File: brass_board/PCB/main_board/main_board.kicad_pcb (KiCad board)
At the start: 2 copper layers, 76 parts, among them J1 Conn_POS_input_B, J10 Conn_Galvo_B, J2 Conn_POS_input_A, J6 Conn_ADC, J8 Conn_01x03_Male_Power, J9 Conn_Galvo_A, Q1 2N2219, U1 LM393, U10 Teensy4.0, U11 Teensy4.0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

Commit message: Added Arduino
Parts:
- added A1: Arduino_Nano_v3.x, Module:Arduino_Nano, F.Cu at (125.9, 146.9)
- added Q2: 2N2219, Package_TO_SOT_THT:TO-39-3, F.Cu at (146.1, 147.8)

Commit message: Added test points and line driver for laser trigger
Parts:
- added J14: Conn_POS_input_A, Connector_PinHeader_2.54mm:PinHeader_1x03_P2.54mm_Vertical, F.Cu at (105.4, 149.3)
- added J15: Conn_POS_input_B, Connector_PinHeader_2.54mm:PinHeader_1x03_P2.54mm_Vertical, F.Cu at (110.0, 149.3)
- added J16: Conn_02x02_Odd_Even, Connector_PinHeader_2.54mm:PinHeader_2x02_P2.54mm_Vertical, F.Cu at (115.0, 126.0)
- added J17: Conn_02x02_Odd_Even, Connector_PinHeader_2.54mm:PinHeader_2x02_P2.54mm_Vertical, F.Cu at (33.6, 87.8)
- added J18: Conn_02x02_Odd_Even, Connector_PinHeader_2.54mm:PinHeader_2x02_P2.54mm_Vertical, F.Cu at (33.6, 95.0)
- added J20: Conn_ADC, Connector_PinHeader_2.54mm:PinHeader_1x03_P2.54mm_Vertical, F.Cu at (38.2, 78.1)
- added J21: Conn_02x02_Odd_Even, Connector_PinHeader_2.54mm:PinHeader_2x02_P2.54mm_Vertical, F.Cu at (52.2, 78.1)
- added J22: Conn_01x03_Male_Power, Connector_PinHeader_2.54mm:PinHeader_1x03_P2.54mm_Vertical, F.Cu at (33.6, 78.1)
- added J23: Conn_02x02_Odd_Even, Connector_PinHeader_2.54mm:PinHeader_2x02_P2.54mm_Vertical, F.Cu at (40.8, 87.8)
- added J24: Conn_02x02_Odd_Even, Connector_PinHeader_2.54mm:PinHeader_2x02_P2.54mm_Vertical, F.Cu at (26.4, 131.0)
- added J25: Conn_Galvo_A, Connector_PinHeader_2.54mm:PinHeader_1x03_P2.54mm_Vertical, F.Cu at (42.9, 78.1)
- added J26: Conn_Galvo_B, Connector_PinHeader_2.54mm:PinHeader_1x03_P2.54mm_Vertical, F.Cu at (47.5, 78.1)
- added J27: Conn_01x40_Male, Connector_PinHeader_2.54mm:PinHeader_2x20_P2.54mm_Vertical, F.Cu at (18.8, 78.1)
- added J3: Conn_01x40_Male, Connector_PinHeader_2.54mm:PinHeader_2x20_P2.54mm_Vertical, F.Cu at (26.4, 78.1)
- added U15: TLV3201, Package_TO_SOT_SMD:SOT-23-5, F.Cu at (41.0, 94.9)
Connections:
- J10 pad 2: Net-(U5-Pad1) -> Net-(J10-Pad2)
- J10 pad 3: Net-(U4-Pad7) -> Net-(J10-Pad3)
- J9 pad 2: Net-(U5-Pad7) -> Net-(J9-Pad2)
- J9 pad 3: Net-(U1-Pad7) -> Net-(J9-Pad3)
- R16 pad 1: Net-(J6-Pad1) -> Net-(R16-Pad1)
- R18 pad 1: Net-(J6-Pad3) -> Net-(R18-Pad1)
- U2 pad 3: Net-(J2-Pad1) -> Net-(U2-Pad3)
- U2 pad 5: Net-(J2-Pad3) -> Net-(U2-Pad5)
- U3 pad 3: Net-(J1-Pad1) -> Net-(U3-Pad3)
- U3 pad 5: Net-(J1-Pad3) -> Net-(U3-Pad5)

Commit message: First PCB placement
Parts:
- added C1: C_Small, Capacitor_SMD:C_0603_1608Metric, F.Cu at (17.8, 144.9)
- added C10: C_Small, Capacitor_SMD:C_0603_1608Metric, F.Cu at (46.9, 15.3)
- added C11: C_Small, Capacitor_SMD:C_0603_1608Metric, F.Cu at (33.8, 17.4)
- added C12: C_Small, Capacitor_SMD:C_0603_1608Metric, F.Cu at (33.8, 21.2)
- added C13: C_Small, Capacitor_SMD:C_0603_1608Metric, F.Cu at (46.4, 19.4)
- added C2: C_Small, Capacitor_SMD:C_0603_1608Metric, F.Cu at (17.8, 147.4)
- added C3: C_Small, Capacitor_SMD:C_0603_1608Metric, F.Cu at (-34.2, 99.6)
- added C4: C_Small, Capacitor_SMD:C_0603_1608Metric, F.Cu at (-34.3, 104.6)
- added C5: C_Small, Capacitor_SMD:C_0603_1608Metric, F.Cu at (133.4, -16.0)
- added C6: C_Small, Capacitor_SMD:C_0603_1608Metric, F.Cu at (139.0, -14.9)
- added C7: C_Small, Capacitor_SMD:C_0603_1608Metric, F.Cu at (139.0, -19.6)
- added C8: C_Small, Capacitor_SMD:C_0603_1608Metric, F.Cu at (85.5, -30.9)
- added C9: C_Small, Capacitor_SMD:C_0603_1608Metric, F.Cu at (84.4, -23.4)
- added FB1: FerriteBead_Small, Resistor_SMD:R_0805_2012Metric, F.Cu at (-44.1, 97.4)
- added FB2: FerriteBead_Small, Resistor_SMD:R_0805_2012Metric, F.Cu at (-45.2, 101.3)
- added FB3: FerriteBead_Small, Resistor_SMD:R_0805_2012Metric, F.Cu at (-42.6, 104.5)
- added J11: Conn_OLED, Connector_PinHeader_2.54mm:PinHeader_1x04_P2.54mm_Vertical, F.Cu at (22.2, 14.6)
- added J12: Conn_LED_CTL, Connector_PinHeader_2.54mm:PinHeader_1x02_P2.54mm_Vertical, F.Cu at (159.9, -17.8)
- added J13: Conn_Laser_Trigger, Connector_PinHeader_2.54mm:PinHeader_1x02_P2.54mm_Vertical, F.Cu at (169.6, 121.1)
- added J19: Conn_ADC, Connector_PinHeader_2.54mm:PinHeader_1x04_P2.54mm_Vertical, F.Cu at (87.6, 170.5)
- added J4: Conn_01x04_Male, Connector_PinHeader_2.54mm:PinHeader_1x04_P2.54mm_Vertical, F.Cu at (163.4, 42.4)
- added J5: Conn_ADC, Connector_PinHeader_2.54mm:PinHeader_2x02_P2.54mm_Vertical, F.Cu at (94.6, 165.1)
- added J7: Conn_LED_PWM, Connector_PinHeader_2.54mm:PinHeader_1x02_P2.54mm_Vertical, F.Cu at (110.7, -20.8)
- added R44: R_Small_US, Resistor_SMD:R_0603_1608Metric, F.Cu at (180.5, 111.0)
- added R45: R_Small_US, Resistor_SMD:R_0603_1608Metric, F.Cu at (192.0, 99.1)
- added R46: R_Small_US, Resistor_SMD:R_0603_1608Metric, F.Cu at (185.7, 129.3)
- added R47: R_Small_US, Resistor_SMD:R_0603_1608Metric, F.Cu at (168.7, 133.7)
- added TP1: TestPoint, Connector_PinHeader_2.54mm:PinHeader_1x01_P2.54mm_Vertical, F.Cu at (148.4, 38.3)
- added TP2: TestPoint, Connector_PinHeader_2.54mm:PinHeader_1x01_P2.54mm_Vertical, F.Cu at (112.8, -32.7)
- added TP3: TestPoint, Connector_PinHeader_2.54mm:PinHeader_1x01_P2.54mm_Vertical, F.Cu at (125.9, -32.7)
- added TP4: TestPoint, Connector_PinHeader_2.54mm:PinHeader_1x01_P2.54mm_Vertical, F.Cu at (142.5, -23.2)
- added TP5: TestPoint, Connector_PinHeader_2.54mm:PinHeader_1x01_P2.54mm_Vertical, F.Cu at (134.8, -24.8)
- Q1, Q2: value 2N2219 -> MMBT3904; footprint Package_TO_SOT_THT:TO-39-3 -> Package_TO_SOT_SMD:SOT-23
- R10, R11, R12, R16, R17, R18, R19, R9: footprint Resistor_SMD:R_0201_0603Metric -> Resistor_SMD:R_0603_1608Metric
- U1, U14, U2, U3, U4, U5, U6, U7: footprint Package_SO:Diodes_PSOP-8 -> Package_SO:SOIC-8-1EP_3.9x4.9mm_P1.27mm_EP2.29x3mm
- U11: footprint teensy:Teensy40_SMT -> teensy:Teensy30_31_32_All_Pins
- moved J24 414.3 mm to (323.9, -157.3)
- moved J9 409.4 mm to (335.9, -166.7)
- moved R34 397.5 mm to (271.4, -172.6)
- moved R24 381.2 mm to (272.9, -169.2)
- moved R35 378.2 mm to (276.0, -157.0)
- moved J25 378.0 mm to (330.9, -166.7)
- moved R21 378.0 mm to (254.8, -157.2)
- moved R23 375.0 mm to (268.4, -171.0)
- moved R25 373.4 mm to (267.6, -164.3)
- moved R22 370.3 mm to (277.2, -173.4)
- moved R27 366.7 mm to (271.8, -155.3)
- moved J26 365.4 mm to (338.1, -143.4)
- moved R26 365.0 mm to (271.5, -157.9)
- moved R20 364.2 mm to (254.6, -146.8)
- moved J23 363.8 mm to (323.1, -141.7)
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
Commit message: Placement done
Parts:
- added C14: 100uF, Capacitor_SMD:C_1210_3225Metric, F.Cu at (25.4, 20.3)
- added C15: 100uF, Capacitor_SMD:C_1210_3225Metric, F.Cu at (33.0, 20.3)
- added C16: 100uF, Capacitor_SMD:C_1210_3225Metric, F.Cu at (114.3, 86.4)
- added C17: 100uF, Capacitor_SMD:C_1210_3225Metric, F.Cu at (114.3, 91.4)
- added C18: 100uF, Capacitor_SMD:C_1210_3225Metric, F.Cu at (107.3, 106.7)
- added C19: 100uF, Capacitor_SMD:C_1210_3225Metric, F.Cu at (107.3, 101.6)
- added C20: 100uF, Capacitor_SMD:C_1210_3225Metric, F.Cu at (62.5, 25.4)
- added C21: 100uF, Capacitor_SMD:C_1210_3225Metric, F.Cu at (62.5, 30.5)
- J20, J6: value Conn_ADC -> Conn_DAC
- U11: footprint teensy:Teensy30_31_32_All_Pins -> teensy:Teensy40
- moved J9 409.1 mm to (73.7, 147.3), turned to 90 degrees
- moved J26 403.4 mm to (58.4, 147.3), turned to 90 degrees
- moved J25 402.0 mm to (73.7, 142.2), turned to 90 degrees
- moved J10 396.3 mm to (58.4, 142.2), turned to 90 degrees
- moved J24 381.2 mm to (78.7, 134.6), turned to -90 degrees
- moved J23 379.1 mm to (63.5, 134.6), turned to -90 degrees
- moved U5 366.6 mm to (71.1, 132.1), turned to -90 degrees
- moved R22 360.4 mm to (69.8, 121.3), turned to -90 degrees
- moved R34 359.7 mm to (76.2, 129.5)
- moved R23 352.3 mm to (71.8, 121.3), turned to -90 degrees
- moved R24 351.6 mm to (82.5, 126.4), turned to -90 degrees
- moved R35 350.2 mm to (71.1, 127.0)
- moved R26 347.0 mm to (69.8, 124.5), turned to -90 degrees
- moved R25 345.6 mm to (80.6, 126.4), turned to -90 degrees
- moved R36 344.7 mm to (63.5, 129.5)
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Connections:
- J23 pad 3: Net-(U5-Pad1) -> Net-(J23-Pad3)
- J24 pad 3: Net-(U5-Pad7) -> Net-(J24-Pad3)
- R25 pad 2: Net-(U5-Pad5) -> Net-(R25-Pad2)
- R26 pad 2: Net-(U5-Pad5) -> Net-(R25-Pad2)
- R27 pad 2: Net-(U5-Pad6) -> Net-(R27-Pad2)
- R31 pad 2: Net-(U5-Pad3) -> Net-(R31-Pad2)
- R32 pad 2: Net-(U5-Pad3) -> Net-(R31-Pad2)
- R33 pad 2: Net-(U5-Pad2) -> Net-(R33-Pad2)
- R35 pad 1: Net-(U5-Pad6) -> Net-(R27-Pad2)
- R35 pad 2: Net-(U5-Pad7) -> Net-(J24-Pad3)
- R37 pad 1: Net-(U5-Pad2) -> Net-(R33-Pad2)
- R37 pad 2: Net-(U5-Pad1) -> Net-(J23-Pad3)
- U5 pad 1: Net-(U5-Pad1) -> Net-(J24-Pad3)
- U5 pad 2: Net-(U5-Pad2) -> Net-(R27-Pad2)
- U5 pad 3: Net-(U5-Pad3) -> Net-(R25-Pad2)
- U5 pad 5: Net-(U5-Pad5) -> Net-(R31-Pad2)
- U5 pad 6: Net-(U5-Pad6) -> Net-(R33-Pad2)
- U5 pad 7: Net-(U5-Pad7) -> Net-(J23-Pad3)
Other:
- board outline added: 104.1 x 147.3 mm

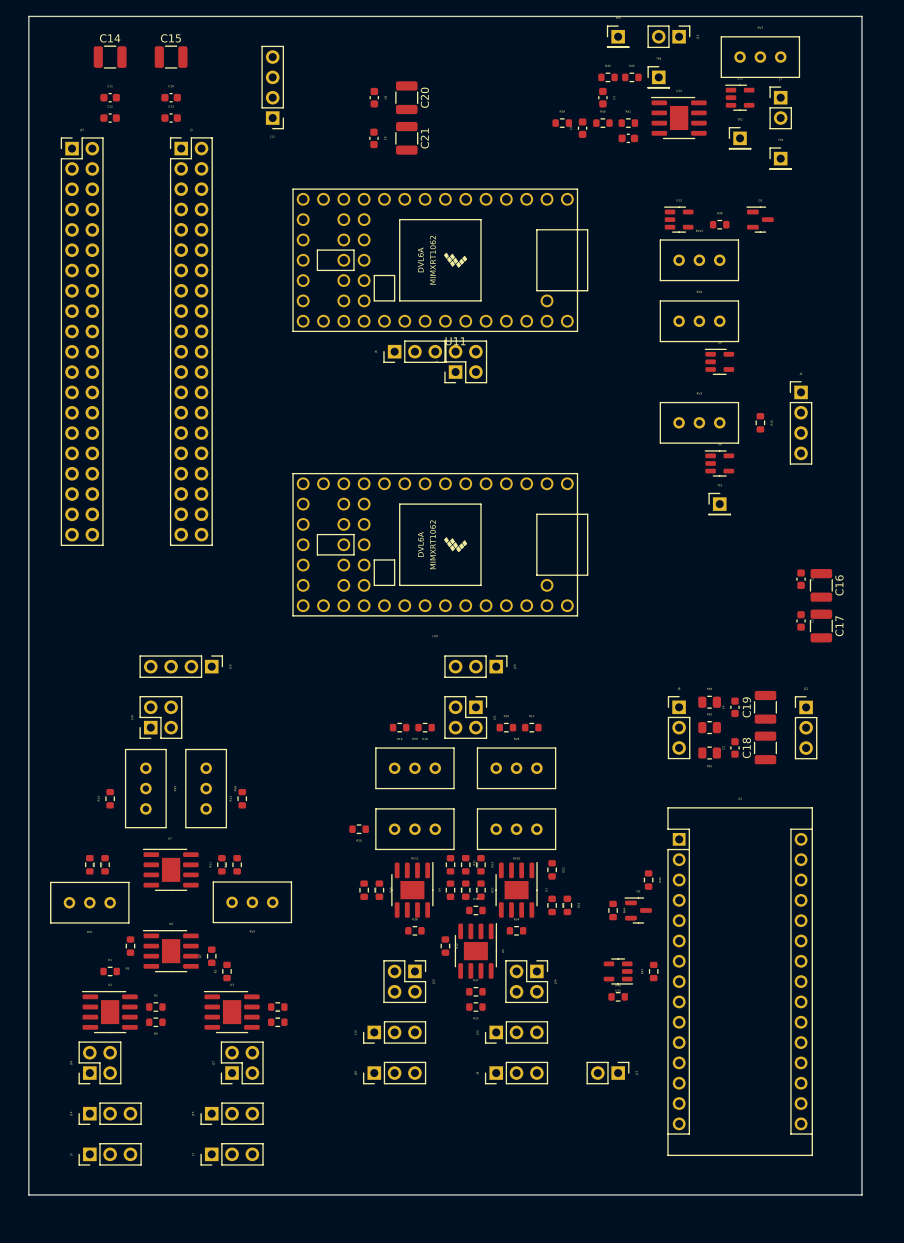
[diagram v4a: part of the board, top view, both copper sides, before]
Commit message: Added LTspice tests and fixed error on opamp. ready for routing
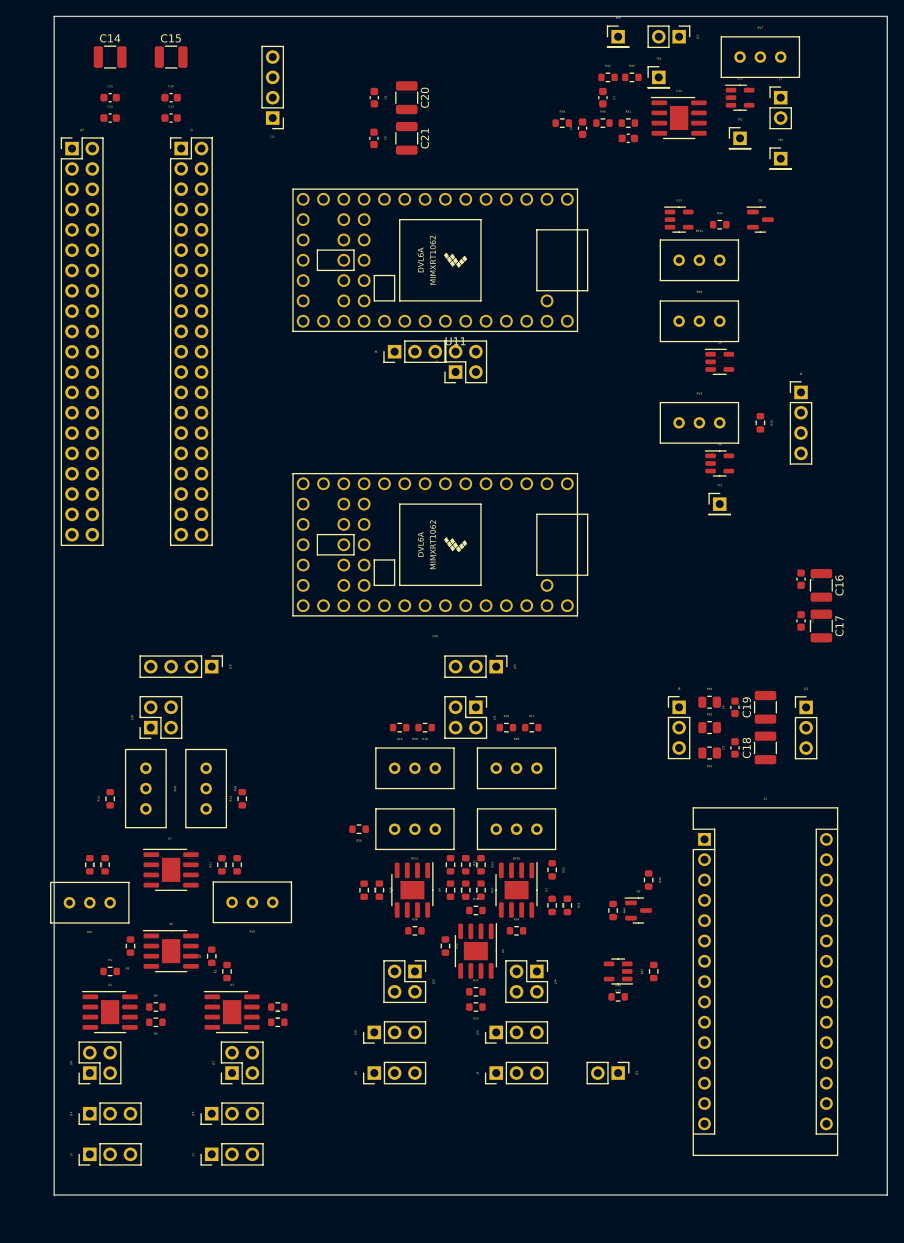
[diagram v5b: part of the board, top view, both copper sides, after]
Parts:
- moved A1 3.16 mm to (99.7, 118.1)
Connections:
- R5 pad 2: Net-(R5-Pad2) -> GND
- R6 pad 2: GND -> Net-(R9-Pad1)
- R7 pad 2: Net-(R11-Pad1) -> GND
- R8 pad 2: GND -> Net-(R11-Pad1)
- R9 pad 1: Net-(R5-Pad2) -> Net-(R9-Pad1)
- U6 pad 1: Net-(R5-Pad2) -> Net-(R9-Pad1)
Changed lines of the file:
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@@
   (net 18 "Net-(R4-Pad1)")
   (net 19 "Net-(R4-Pad2)")
-  (net 20 "Net-(R5-Pad2)")
+  (net 20 "Net-(R9-Pad1)")
   (net 21 "Net-(R11-Pad1)")
   (net 22 "Net-(R10-Pad1)")
@@
       (net 13 "Net-(R1-Pad2)") (pintype "passive"))
     (pad "2" smd roundrect (at 0.825 0 90) (size 0.8 0.95) (layers "F.Cu" "F.Paste" "F.Mask") (roundrect_rratio 0.25)
-      (net 20 "Net-(R5-Pad2)") (pintype "passive"))
+      (net 2 "GND") (pintype "passive"))
     (model "${KICAD6_3DMODEL_DIR}/Resistor_SMD.3dshapes/R_0603_1608Metric.wrl"
       (offset (xyz 0 0 0))
@@
       (net 19 "Net-(R4-Pad2)") (pintype "passive"))
     (pad "2" smd roundrect (at 0.825 0) (size 0.8 0.95) (layers "F.Cu" "F.Paste" "F.Mask") (roundrect_rratio 0.25)
-      (net 2 "GND") (pintype "passive"))
+      (net 21 "Net-(R11-Pad1)") (pintype "passive"))
     (model "${KICAD6_3DMODEL_DIR}/Resistor_SMD.3dshapes/R_0603_1608Metric.wrl"
       (offset (xyz 0 0 0))
@@
     (fp_line (start 0.8 0.4125) (end -0.8 0.4125) (layer "F.Fab") (width 0.1))
     (pad "1" smd roundrect (at -0.825 0 90) (size 0.8 0.95) (layers "F.Cu" "F.Paste" "F.Mask") (roundrect_rratio 0.25)
-      (net 20 "Net-(R5-Pad2)") (pintype "passive"))
+      (net 20 "Net-(R9-Pad1)") (pintype "passive"))
     (pad "2" smd roundrect (at 0.825 0 90) (size 0.8 0.95) (layers "F.Cu" "F.Paste" "F.Mask") (roundrect_rratio 0.25)
       (net 22 "Net-(R10-Pad1)") (pintype "passive"))
@@
       (net 17 "Net-(R3-Pad2)") (pintype "passive"))
     (pad "2" smd roundrect (at 0.825 0 90) (size 0.8 0.95) (layers "F.Cu" "F.Paste" "F.Mask") (roundrect_rratio 0.25)
-      (net 21 "Net-(R11-Pad1)") (pintype "passive"))
+      (net 2 "GND") (pintype "passive"))
     (model "${KICAD6_3DMODEL_DIR}/Resistor_SMD.3dshapes/R_0603_1608Metric.wrl"
       (offset (xyz 0 0 0))
@@
       (net 15 "Net-(R2-Pad2)") (pintype "passive"))
     (pad "2" smd roundrect (at 0.825 0 180) (size 0.8 0.95) (layers "F.Cu" "F.Paste" "F.Mask") (roundrect_rratio 0.25)
-      (net 2 "GND") (pintype "passive"))
+      (net 20 "Net-(R9-Pad1)") (pintype "passive"))
     (model "${KICAD6_3DMODEL_DIR}/Resistor_SMD.3dshapes/R_0603_1608Metric.wrl"
       (offset (xyz 0 0 0))
@@
     (pad "" smd roundrect (at 0.57 -0.75) (size 0.92 1.21) (layers "F.Paste") (roundrect_rratio 0.25))
     (pad "1" smd roundrect (at -2.475 -1.905) (size 1.95 0.6) (layers "F.Cu" "F.Paste" "F.Mask") (roundrect_rratio 0.25)
-      (net 20 "Net-(R5-Pad2)") (pintype "open_collector"))
+      (net 20 "Net-(R9-Pad1)") (pintype "open_collector"))
     (pad "2" smd roundrect (at -2.475 -0.635) (size 1.95 0.6) (layers "F.Cu" "F.Paste" "F.Mask") (roundrect_rratio 0.25)
       (net 15 "Net-(R2-Pad2)") (pinfunction "-") (pintype "input"))
@@
       (effects (font (size 0.254 0.254) (thickness 0.0508)))
     )
-    (fp_text value "R_Small_US" (at 0 1.43 90) (layer "F.Fab")
+    (fp_text value "R_Small_US" (at 0 4.595 90) (layer "F.Fab")
       (effects (font (size 0.254 0.254) (thickness 0.0508)))
     )
@@
   )
   (footprint "Module:Arduino_Nano" (layer "F.Cu")
-    (at 96.53 118.11)
+    (at 99.695 118.11)
     (descr "Arduino Nano, http://www.mouser.com/pdfdocs/Gravitech_Arduino_Nano3_0.pdf")
     (tags "Arduino Nano")
@@
     )
   )
-  (gr_rect (start 119.38 162.56) (end 15.24 15.24) (layer "Edge.Cuts") (width 0.1) (fill none))
+  (gr_rect (start 122.545 162.56) (end 18.405 15.24) (layer "Edge.Cuts") (width 0.1) (fill none))
   (group "" (id 3ff670cd-ffb3-439b-9af1-d73390668826)
     (members
